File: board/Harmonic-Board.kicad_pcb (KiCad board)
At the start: 4 copper layers, 45 x 35.5 mm, 90 parts, among them SW1 SW_Push, SW2 SW_Push, SW3 SW_Push, SW4 SW_Push, SW5 DNP, SW6 DNP, SW7 DNP, T1 2N7002, T2 BSS215P, T3 BSS215P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

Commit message: worked on schematics: - added new display - delete unwanted parts
Work on PCB:
- cleaned old pcb routes
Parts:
- removed C1, C2: 10pF, Capacitor_SMD:C_0201_0603Metric
- removed C3, C7: 22µF, Capacitor_SMD:C_0603_1608Metric
- removed C4, C6: 100nF, Capacitor_SMD:C_0201_0603Metric
- removed C5, C8: 1µF, Capacitor_SMD:C_0402_1005Metric
- removed Disp1: ST7735_IPS_Display, china:KD0096FM-1
- removed LED10, LED11, LED12, LED13, LED14, LED15, LED5, LED6, LED7, LED8, LED9: SK9822-2020, china:SK9822
- removed LOGO2: Logo_Open_Hardware_Large, badge:artwork-top-2
- removed LOGO4: Logo_Open_Hardware_Large, badge:artwork-top-3
- removed R1, R2, R3, R8: 0, Resistor_SMD:R_0201_0603Metric
- removed R18: 6.8, Resistor_SMD:R_0402_1005Metric
- removed R25: 1M, Resistor_SMD:R_0201_0603Metric
- removed R4, R7: DNP, Resistor_SMD:R_0201_0603Metric
- removed R5, R6, R9: 49.9k, Resistor_SMD:R_0201_0603Metric
- removed SW5, SW6, SW7: DNP, china:EVQP7J01P
- removed T2: BSS215P, Package_TO_SOT_SMD:SOT-23
- removed TP1: ECG_N, TestPoint:TestPoint_THTPad_D2.0mm_Drill1.0mm
- removed TP2: ECG_P, TestPoint:TestPoint_THTPad_D2.0mm_Drill1.0mm
- removed TP3, TP4, TP5, TP6, TP7, TP8: TestPoint, TestPoint:TestPoint_Keystone_5015_Micro-Minature
- removed U1: MAX86150EFF+T, maxim:MAX86150
- added C11: 100nF, Capacitor_SMD:C_0201_0603Metric, F.Cu at (119.8, 67.1)
- added C12: 10uF, Capacitor_SMD:C_0201_0603Metric, F.Cu at (109.0, 74.2)
- added C13: 10uF, Capacitor_SMD:C_0201_0603Metric, F.Cu at (119.8, 68.8)
- added C14: 100nF, Capacitor_SMD:C_0201_0603Metric, F.Cu at (111.4, 74.2)
- added C15: 1uF, Capacitor_SMD:C_0201_0603Metric, F.Cu at (109.0, 75.9)
- added C16: 10uF, Capacitor_SMD:C_0201_0603Metric, F.Cu at (122.2, 67.1)
- added C17: 10uF, Capacitor_SMD:C_0201_0603Metric, F.Cu at (111.4, 75.9)
- added C18: 10uF, Capacitor_SMD:C_0201_0603Metric, F.Cu at (113.9, 74.2)
- added C19: 10uF, Capacitor_SMD:C_0201_0603Metric, F.Cu at (119.8, 70.6)
- added C20: 330pF, Capacitor_SMD:C_0201_0603Metric, F.Cu at (113.9, 75.9)
- added C21: 10uF, Capacitor_SMD:C_0201_0603Metric, F.Cu at (122.2, 68.8)
- added L1: 10uH, Inductor_SMD:L_0805_2012Metric_Pad1.15x1.40mm_HandSolder, F.Cu at (116.7, 86.0)
- added R23: 1M, Resistor_SMD:R_0201_0603Metric, F.Cu at (124.7, 67.1)
- added R24: 93,1k, Resistor_SMD:R_0201_0603Metric, F.Cu at (119.8, 72.3)
- added R26: 10k, Resistor_SMD:R_0201_0603Metric, F.Cu at (122.2, 70.6)
- added R27: 100k, Resistor_SMD:R_0201_0603Metric, F.Cu at (116.3, 75.9)
- added U3: LT1935ES5-TRMPBF, LT1935:LT1935ES5-TRMPBF, F.Cu at (104.0, 94.7)
- D2: value DNP -> 1N4148; footprint china:side-LED -> Diode_SMD:D_SOD-123; moved to F.Cu
- D3: value DNP -> 1N4148; footprint LED_SMD:LED_0603_1608Metric -> Diode_SMD:D_SOD-123
- R20: value 49.9k -> 1M; moved to F.Cu
- moved D2 66.9 mm to (109.3, 71.5), turned to 0 degrees
- moved D3 45.1 mm to (109.3, 68.0), turned to 0 degrees
- moved R20 31.9 mm to (116.3, 74.2), turned to 0 degrees
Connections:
- D2 pad 1: Net-(D1-Pad1) -> Net-(D2-Pad1)
- D2 pad 2: +3V3 -> Net-(D2-Pad2)
- D3 pad 1: Net-(D3-Pad1) -> GND
- D3 pad 2: +3V3 -> Net-(D2-Pad1)
- D4 pad 2: Net-(D3-Pad1) -> Net-(D4-Pad2)
- LED1 pad 1: Net-(LED1-Pad1) -> RGB_LED_Data
- LED1 pad 2: GND -> RGB_LED_CLK
- LED1 pad 3: RGB_LED_Data -> GND
- LED1 pad 4: RGB_LED_CLK -> Net-(LED1-Pad4)
- LED2 pad 1: Net-(LED2-Pad1) -> Net-(LED1-Pad6)
- LED2 pad 2: GND -> Net-(LED1-Pad5)
- LED2 pad 3: Net-(LED1-Pad1) -> GND
- LED2 pad 4: Net-(LED1-Pad6) -> Net-(LED2-Pad4)
- LED3 pad 1: Net-(LED3-Pad1) -> Net-(LED2-Pad6)
- LED3 pad 2: GND -> Net-(LED2-Pad5)
- LED3 pad 3: Net-(LED2-Pad1) -> GND
- LED3 pad 4: Net-(LED2-Pad6) -> Net-(LED2-Pad4)
- LED3 pad 5: Net-(LED2-Pad5) -> Net-(LED3-Pad5)
- LED4 pad 1: Net-(LED4-Pad1) -> Net-(LED3-Pad6)
- LED4 pad 2: GND -> Net-(LED3-Pad5)
- LED4 pad 3: Net-(LED3-Pad1) -> GND
- LED4 pad 4: Net-(LED3-Pad6) -> Net-(LED2-Pad4)
- LED4 pad 5: Net-(LED2-Pad5) -> (no net)
- LED4 pad 6: Net-(LED4-Pad6) -> (no net)
- R10 pad 1: ECG_N -> (no net)
- R11 pad 1: ECG_P_SWITCHED_WRIST -> (no net)
- R14 pad 1: Net-(D3-Pad1) -> Net-(D4-Pad2)
- R20 pad 1: VSYS -> GND
- R20 pad 2: IO-E-P1 -> (no net)
- T1 pad 3: Net-(R18-Pad1) -> (no net)
- T3 pad 3: Net-(LED1-Pad5) -> Net-(LED1-Pad4)
- T4 pad 3: Net-(LED2-Pad5) -> Net-(LED2-Pad4)
- U2 pad 3: IO-E-P1 -> (no net)
- X2 pad 10: GPIO1 -> (no net)
- X2 pad 20: PMIC_GPIO -> (no net)
- X2 pad 22: GPIO2 -> (no net)
- X2 pad 23: SPI_CS -> (no net)
- X2 pad 24: SPI_MOSI -> (no net)
- X2 pad 25: GPIO6-MISO -> (no net)
- X2 pad 26: SPI_SCK -> (no net)
- X2 pad 5: MAX86150_INT -> (no net)
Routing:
- net +3V3: track 152.6 -> 0.00 mm, vias 10 -> 0
- net GND: track 131.5 -> 0.00 mm, vias 143 -> 0
- net +1V8: track 96.3 -> 0.00 mm, vias 6 -> 0
- net Net-(LED2-Pad5): track 87.3 -> 0.00 mm, vias 6 -> 0
- net SDA_1V8: track 67.4 -> 0.00 mm, vias 4 -> 0
- net SCL_3V3: track 66.9 -> 0.00 mm, vias 2 -> 0
- net SCL_1V8: track 62.6 -> 0.00 mm, vias 4 -> 0
- net SDA_3V3: track 59.6 -> 0.00 mm, vias 3 -> 0
- net ECG_N: track 58.6 -> 0.00 mm, vias 2 -> 0
- net GPIO2: track 57.7 -> 0.00 mm, vias 4 -> 0
- net IO-E-P3: track 55.3 -> 0.00 mm, vias 4 -> 0
- net GPIO5: track 55.2 -> 0.00 mm, vias 3 -> 0
- net RGB_LED_CLK: track 51.0 -> 0.00 mm, vias 3 -> 0
- net MAX86150_INT: track 49.9 -> 0.00 mm, vias 3 -> 0
- net RGB_LED_Data: track 48.4 -> 0.00 mm, vias 2 -> 0
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- removed copper zone on F.Cu, net ECG_N
- removed copper zone on F.Cu, net ECG_P_SWITCHED_WRIST
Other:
- board text removed: "ECG2"

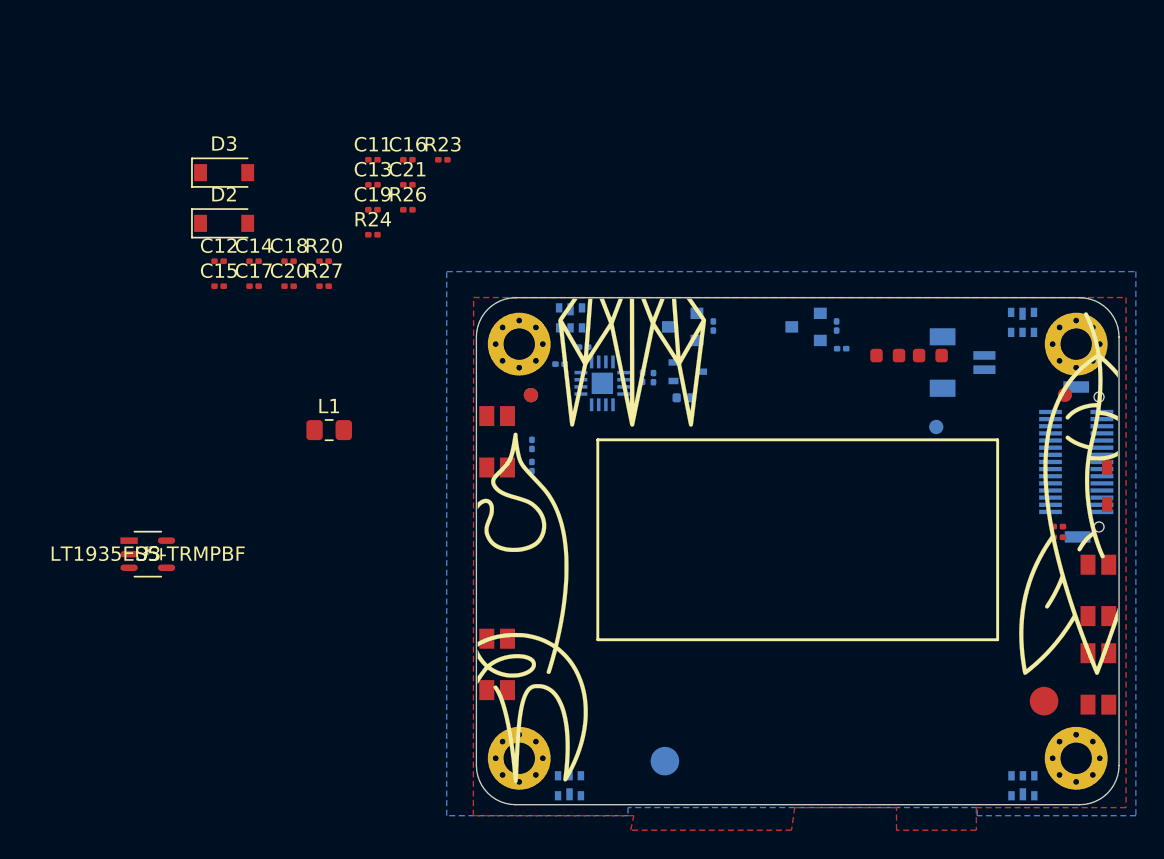
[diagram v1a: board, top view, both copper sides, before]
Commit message: - Added connector lib - added footprint for schottkey diode - added keep-out for new display
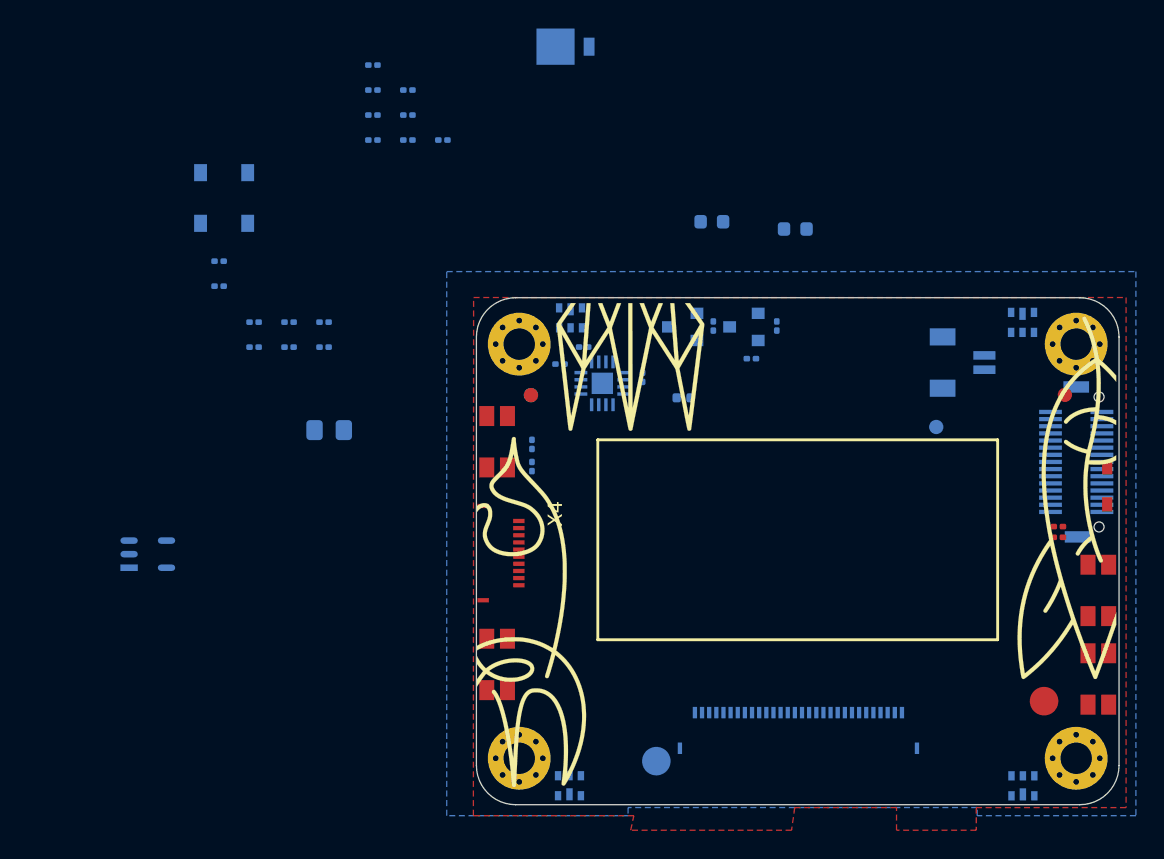
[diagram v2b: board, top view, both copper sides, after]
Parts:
- removed LOGO3: Logo_Open_Hardware_Large, badge:artwork-top
- removed R19: 49.9k, Resistor_SMD:R_0201_0603Metric
- removed T1: 2N7002, Package_TO_SOT_SMD:SOT-323_SC-70
- added D5: SS2P6-M3/84A, badge:DO-220AA, B.Cu at (132.5, 59.2)
- added LOGO4: Logo_Open_Hardware_Large, badge:artwork-top, F.Cu at (149.4, 87.7)
- added X3: 687130182122, WR-FPC 0.50 mm SMT ZIF Horizontal Dual Contact:687130182122, B.Cu at (151.8, 103.8)
- added X4: 687106182122, WR-FPC 0.50 mm SMT ZIF Horizontal Dual Contact:687110182122, F.Cu at (128.5, 94.7)
- C11, C12, C13, C14, C15, C16, C17, C18, C19, C20, C21, D2, D3, D4, L1, R14, R20, R23, R24, R26, R27, U3: moved to B.Cu
- moved R14 15.5 mm to (143.5, 71.4)
- moved D4 13.0 mm to (149.3, 71.9)
- moved R24 11.9 mm to (119.8, 60.5)
- moved C19 8.38 mm to (119.8, 62.2)
- moved R26 8.38 mm to (122.2, 62.2)
- moved C10 6.36 mm to (146.3, 81.0), turned to 180 degrees
- moved C14 6.02 mm to (111.4, 80.2)
- moved C18 6.02 mm to (113.9, 80.2)
- moved R20 6.02 mm to (116.3, 80.2)
- moved C13 4.88 mm to (119.8, 64.0)
- moved C21 4.88 mm to (122.2, 64.0)
- moved T4 4.35 mm to (145.7, 78.8)
- moved R22 4.19 mm to (148.0, 78.7)
- moved C17 2.52 mm to (111.4, 78.5)
- moved C20 2.52 mm to (113.9, 78.5)
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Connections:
- C11 pad 2: (no net) -> Net-(C11-Pad2)
- C12 pad 2: (no net) -> Net-(C12-Pad2)
- R20 pad 2: (no net) -> Net-(R20-Pad2)
- R23 pad 2: (no net) -> Net-(R23-Pad2)
- U2 pad 3: (no net) -> IO-E-P1
- X2 pad 10: (no net) -> GPIO1
- X2 pad 22: (no net) -> GPIO2
- X2 pad 23: (no net) -> SPI_CS
- X2 pad 24: (no net) -> SPI_MOSI
- X2 pad 25: (no net) -> GPIO6-MISO
- X2 pad 26: (no net) -> SPI_SCK
- X2 pad 27: GPIO4 -> (no net)
- X2 pad 5: (no net) -> MAX86150_INT
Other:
- board text added: "Display: ST-2828GDEDF11"
- board text added: "Glue Point"
